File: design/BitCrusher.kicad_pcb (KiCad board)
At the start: 2 copper layers, 181.5 x 86.2 mm, 136 parts, among them J1 BNC, J10 PJ-002BH, J2 BWSMA-KWE-Z001, J3 BWSMA-KE-Z001, J4 BWSMA-KE-Z001, J5 SHOU HAN TYPE-C 14P CC-2.6, J6 Conn_01x04_Pin, J7 Conn_01x04_Pin, J8 Conn_01x03_Pin, J9 Conn_01x03_Pin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

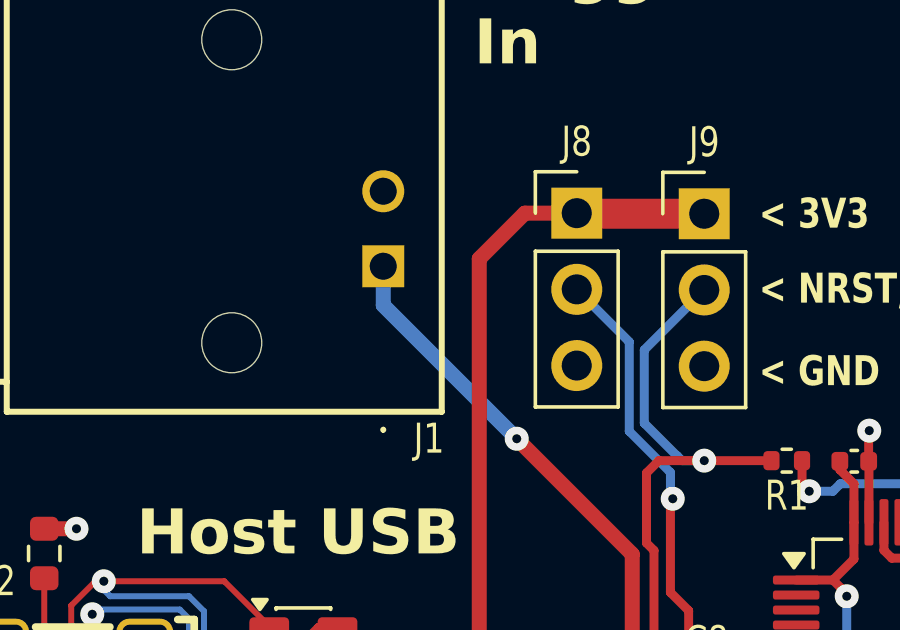
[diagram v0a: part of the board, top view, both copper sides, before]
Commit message: Fixed BNC footprint polarity
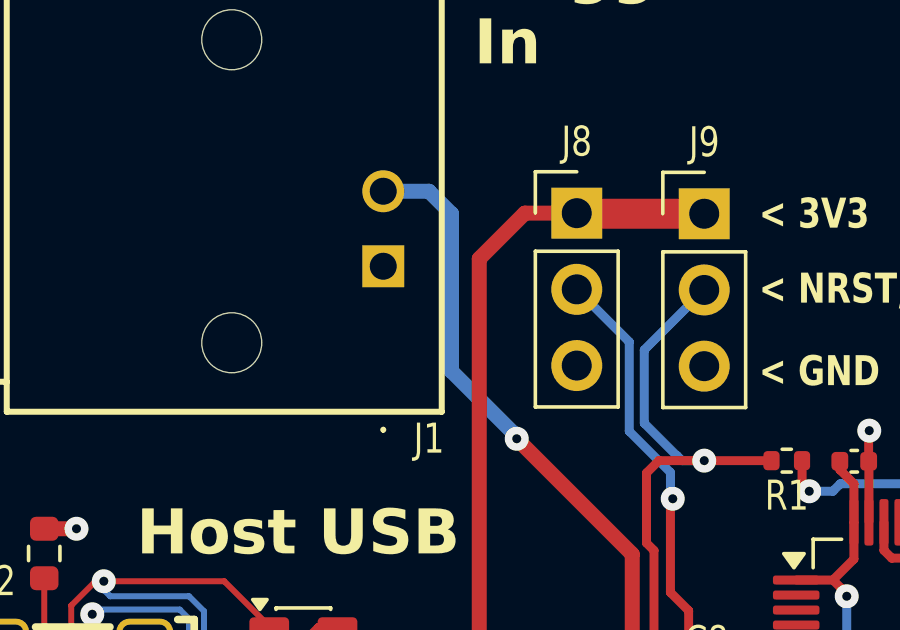
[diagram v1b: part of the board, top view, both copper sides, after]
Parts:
- C14, C16: value 5u -> 1u
- D7: value D_Schottky -> JSCJ B5819W SL
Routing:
- net HWTrig+: track 35.9 -> 39.3 mm
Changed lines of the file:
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@@
 			)
 		)
-		(property "Value" "5u"
+		(property "Value" "1u"
 			(at 0 1.16 270)
 			(unlocked yes)
@@
 		(sheetname "/Control & Interface/")
 		(sheetfile "control.kicad_sch")
-		(units
-			(unit
-				(name "A")
-				(pins "1" "2")
-			)
-		)
 		(attr through_hole)
 		(duplicate_pad_numbers_are_jumpers no)
@@
 			(layers "*.Cu" "*.Mask")
 		)
-		(pad "1" thru_hole rect
-			(at 0 0 90)
+		(pad "1" thru_hole circle
+			(at 2.5 0 90)
 			(size 1.4 1.4)
 			(drill 0.9)
@@
 			(pintype "passive")
 		)
-		(pad "2" thru_hole circle
-			(at 2.5 0 90)
+		(pad "2" thru_hole rect
+			(at 0 0 90)
 			(size 1.4 1.4)
 			(drill 0.9)
@@
 			)
 		)
-		(property "Value" "5u"
+		(property "Value" "1u"
 			(at 0 1.16 270)
 			(unlocked yes)
@@
 			)
 		)
-		(property "Value" "D_Schottky"
+		(property "Value" "JSCJ B5819W SL"
 			(at 0 2.1 270)
 			(unlocked yes)
@@
 	)
 	(segment
-		(start 75.225 84.5)
-		(end 75.225 85.8)
+		(start 79.675 90.175)
+		(end 77.5 88)
 		(width 0.5)
 		(layer "B.Cu")
@@
 	)
 	(segment
+		(start 76.75 82)
+		(end 75.225 82)
+		(width 0.5)
+		(layer "B.Cu")
+		(net "HWTrig+")
+	)
+	(segment
 		(start 83.475 98)
 		(end 83.525 98.05)
@@
 	)
 	(segment
+		(start 77.5 88)
+		(end 77.5 82.75)
+		(width 0.5)
+		(layer "B.Cu")
+		(net "HWTrig+")
+	)
+	(segment
+		(start 79.675 90.25)
+		(end 79.675 90.175)
+		(width 0.5)
+		(layer "B.Cu")
+		(net "HWTrig+")
+	)
+	(segment
 		(start 83.425 98)
 		(end 83.475 98)
@@
 	)
 	(segment
-		(start 75.225 85.8)
-		(end 79.675 90.25)
+		(start 77.5 82.75)
+		(end 76.75 82)
 		(width 0.5)
 		(layer "B.Cu")
